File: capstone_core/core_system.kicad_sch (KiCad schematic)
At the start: 10 parts, among them U2 LSM6DSVTR, U3 ZED F9P GNSS & RTK Module, U4 PCA9306USG

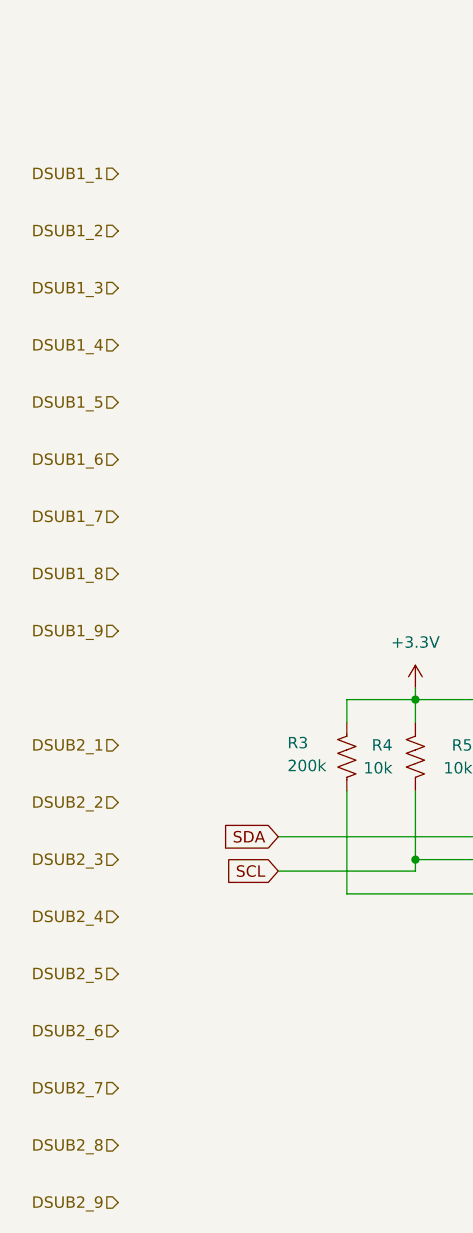
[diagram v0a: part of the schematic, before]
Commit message: moving connectors around
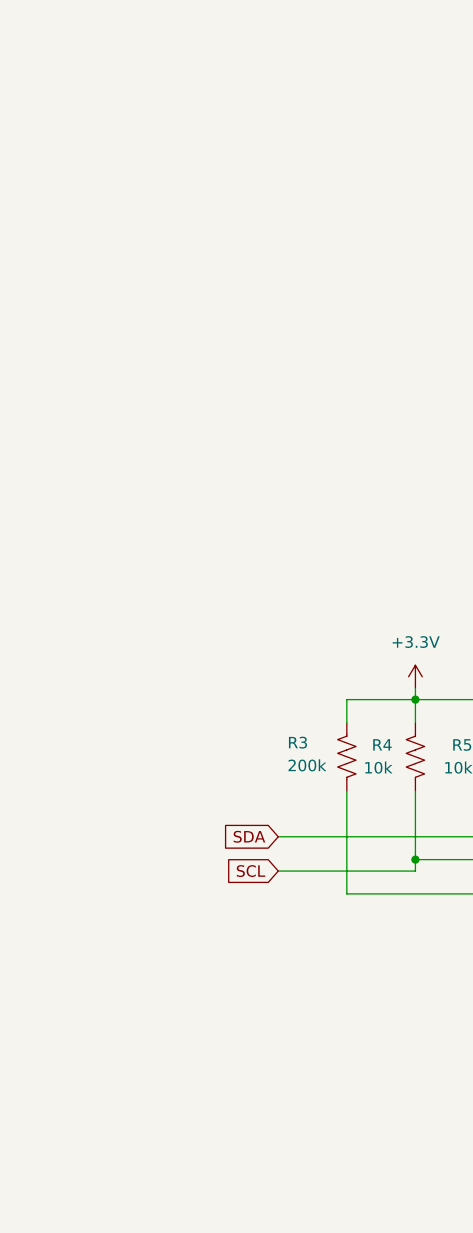
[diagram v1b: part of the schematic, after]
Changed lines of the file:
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@@
-		)
-	)
-	(hierarchical_label "DSUB2_2"
-		(shape input)
-		(at 55.88 121.92 180)
-		(effects
-			(font
-				(size 1.27 1.27)
-			)
-			(justify right)
-		)
-	)
-	(hierarchical_label "DSUB2_7"
-		(shape input)
-		(at 55.88 153.67 180)
-		(effects
-			(font
-				(size 1.27 1.27)
-			)
-			(justify right)
-		)
-	)
-	(hierarchical_label "DSUB1_8"
-		(shape input)
-		(at 55.88 96.52 180)
-		(effects
-			(font
-				(size 1.27 1.27)
-			)
-			(justify right)
-		)
-	)
-	(hierarchical_label "DSUB1_5"
-		(shape input)
-		(at 55.88 77.47 180)
-		(effects
-			(font
-				(size 1.27 1.27)
-			)
-			(justify right)
-		)
-	)
-	(hierarchical_label "DSUB1_3"
-		(shape input)
-		(at 55.88 64.77 180)
-		(effects
-			(font
-				(size 1.27 1.27)
-			)
-			(justify right)
-		)
-	)
-	(hierarchical_label "DSUB1_1"
-		(shape input)
-		(at 55.88 52.07 180)
-		(effects
-			(font
-				(size 1.27 1.27)
-			)
-			(justify right)
-		)
-	)
-	(hierarchical_label "DSUB1_6"
-		(shape input)
-		(at 55.88 83.82 180)
-		(effects
-			(font
-				(size 1.27 1.27)
-			)
-			(justify right)
-		)
-	)
-	(hierarchical_label "DSUB2_8"
-		(shape input)
-		(at 55.88 160.02 180)
-		(effects
-			(font
-				(size 1.27 1.27)
-			)
-			(justify right)
-		)
-	)
-	(hierarchical_label "DSUB2_1"
-		(shape input)
-		(at 55.88 115.57 180)
-		(effects
-			(font
-				(size 1.27 1.27)
-			)
-			(justify right)
-		)
-	)
-	(hierarchical_label "DSUB1_2"
-		(shape input)
-		(at 55.88 58.42 180)
-		(effects
-			(font
-				(size 1.27 1.27)
-			)
-			(justify right)
-		)
-	)
-	(hierarchical_label "DSUB2_5"
-		(shape input)
-		(at 55.88 140.97 180)
-		(effects
-			(font
-				(size 1.27 1.27)
-			)
-			(justify right)
-		)
-	)
-	(hierarchical_label "DSUB1_4"
-		(shape input)
-		(at 55.88 71.12 180)
-		(effects
-			(font
-				(size 1.27 1.27)
-			)
-			(justify right)
-		)
-	)
-	(hierarchical_label "DSUB2_9"
-		(shape input)
-		(at 55.88 166.37 180)
-		(effects
-			(font
-				(size 1.27 1.27)
-			)
-			(justify right)
-		)
-	)
-	(hierarchical_label "DSUB1_7"
-		(shape input)
-		(at 55.88 90.17 180)
-		(effects
-			(font
-				(size 1.27 1.27)
-			)
-			(justify right)
-		)
-	)
-	(hierarchical_label "DSUB1_9"
-		(shape input)
-		(at 55.88 102.87 180)
-		(effects
-			(font
-				(size 1.27 1.27)
-			)
-			(justify right)
-		)
-	)
-	(hierarchical_label "DSUB2_4"
-		(shape input)
-		(at 55.88 134.62 180)
-		(effects
-			(font
-				(size 1.27 1.27)
-			)
-			(justify right)
-		)
-	)
-	(hierarchical_label "DSUB2_3"
-		(shape input)
-		(at 55.88 128.27 180)
-		(effects
-			(font
-				(size 1.27 1.27)
-			)
-			(justify right)
-		)
-	)
-	(hierarchical_label "DSUB2_6"
-		(shape input)
-		(at 55.88 147.32 180)
-		(effects
-			(font
-				(size 1.27 1.27)
-			)
-			(justify right)
 		)
 	)

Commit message: up to date project
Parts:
- renumbered C5 to C15, C4 to C16, R3 to R5, R4 to R6, R5 to R7, R2 to R8, R1 to R9, U4 to U5, U3 to U6, U2 to U7
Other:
- moved on the sheet: C15, C16, R5, R6, R7, R8, R9, U5, U6, U7
